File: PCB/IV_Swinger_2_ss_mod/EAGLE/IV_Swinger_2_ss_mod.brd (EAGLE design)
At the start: 59.7 x 53.3 mm, 33 parts, among them J1 

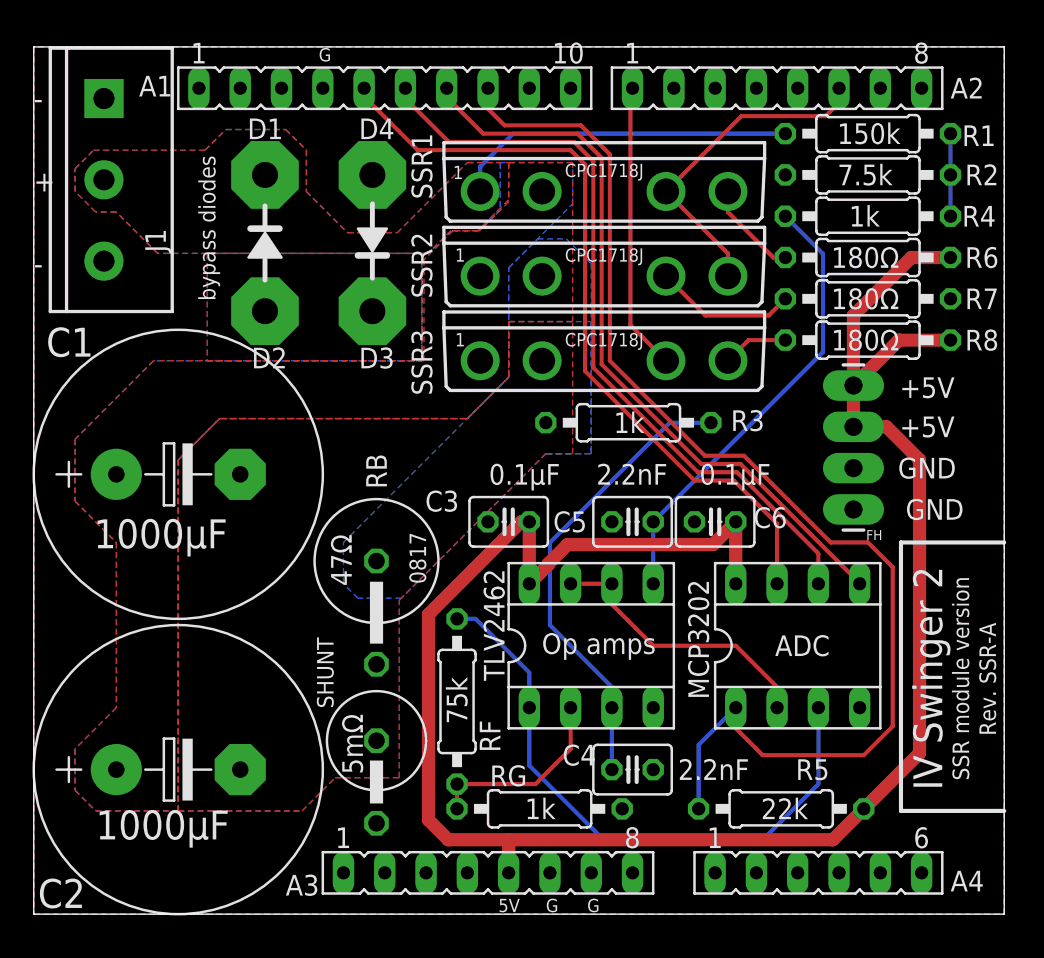
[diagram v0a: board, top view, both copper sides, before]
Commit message: SSR module version PCB, RevB
Fixed bugs in RevA of the SSR module version PCB:

Issue #40: Must drive SSR1 and SSR2 from separate Arduino pins. In the RevA design, there is a path from +5V to GND through the two SSRs, which can cause destruction of the SSRs and the bleed resistor.

Issue #41: Resistor R3 must be connected precisely to the shunt (+) end pad so it doesn't see the voltage at some point in the sea of copper that is the LOAD_CAP- net.  This resulted in current measurements that were too high, and depended on whether the current was flowing from SSR3 or from the load caps.

Issue #41: The path from the shunt (-) end pad to the screw terminal pads must be a stub off the GND plane so that when current is flowing, the GND plane doesn't see a voltage drop.  Also, the linkage between this stub and the GND plane must be made at the shunt (-) end pad so the voltage of the GND plane is equal to the voltage at the (-) end of the shunt.

Also swapped the pads for the bypass diodes for layout reasons related to making the current-carrying part of GND a stub.
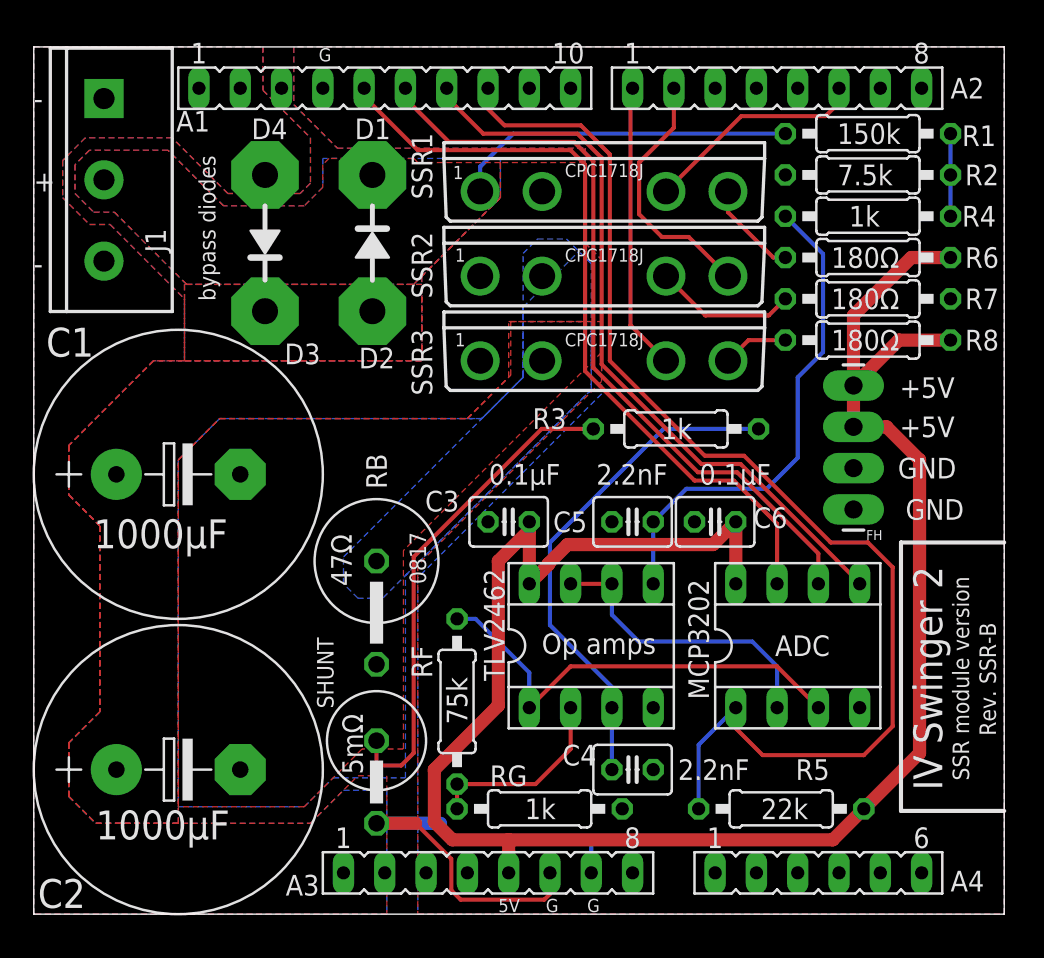
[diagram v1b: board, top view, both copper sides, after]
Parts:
- moved D1 6.60 mm to (20.8, 45.5)
- moved D2 6.60 mm to (20.8, 37.1)
- moved D3 6.60 mm to (14.2, 37.1)
- moved D4 6.60 mm to (14.2, 45.5)
- moved R3 2.95 mm to (39.5, 29.8)
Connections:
- new net N17: RF.2, RG.2, TLV2462.2
- net N1: no longer SSR2.4
- net N10: now also R8.1, SSR3.4; no longer R1.1, R2.2, R4.1
- net N11: now also R1.1, R2.2, R4.1; no longer C5.1, R4.2, TLV2462.5
- net N12: now also C5.1, R4.2, TLV2462.5; no longer MCP3202.2, TLV2462.6, TLV2462.7
- net N13: now also MCP3202.2, TLV2462.6, TLV2462.7; no longer MCP3202.3, RF.1, TLV2462.1
- net N14: now also MCP3202.3, RF.1, TLV2462.1; no longer D2.1, D3.1
- net N15: now also D2.1, D3.1; no longer C4.1, R3.1, TLV2462.3
- net N16: now also C4.1, R3.1, TLV2462.3; no longer RF.2, RG.2, TLV2462.2
- net N2: now also A2.2, SSR2.4; no longer A2.1, SSR3.3
- net N3: now also A2.1, SSR3.3; no longer A1.8, MCP3202.1, R5.1
- net N4: now also A1.8, MCP3202.1, R5.1; no longer A1.7, MCP3202.5
- net N5: now also A1.7, MCP3202.5; no longer A1.6, MCP3202.6
- net N6: now also A1.6, MCP3202.6; no longer A1.5, MCP3202.7
- net N7: now also A1.5, MCP3202.7; no longer R6.1, SSR1.4
- net N8: now also R6.1, SSR1.4; no longer R7.1, SSR2.3
- net N9: now also R7.1, SSR2.3; no longer R8.1, SSR3.4
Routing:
- net N3: track 74.6 -> 17.7 mm
- net N7: track 5.96 -> 47.9 mm
- net GND: track 0.00 -> 30.9 mm
- net LOAD_CAP-: track 0.00 -> 30.5 mm
- net N4: track 45.8 -> 74.6 mm
- net N15: track 28.5 -> 0.00 mm
- net N14: track 0.00 -> 27.9 mm
- net N11: track 27.9 -> 5.08 mm
- net N16: track 11.9 -> 31.3 mm
- net N13: track 37.1 -> 18.5 mm
- net N12: track 17.3 -> 30.8 mm
- net N17: track 0.00 -> 11.9 mm
- net N1: track 20.6 -> 13.8 mm
- net N9: track 4.06 -> 8.77 mm
- net N8: track 8.77 -> 5.96 mm
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- added copper zone on layer 1, net N15
- added copper zone on layer 16, net N15
- removed copper zone on layer 1, net N14
- removed copper zone on layer 16, net N14
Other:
- board text added: "Rev. SSR-B"
- board text removed: "Rev. SSR-A"
